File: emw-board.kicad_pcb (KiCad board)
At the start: 2 copper layers, 49.5 x 48.3 mm, 37 parts, among them P1 1WIRE, P2 BATT, P3 CONN_01X06, P4 SWDN, P5 CONS, P6 OLED, P7 CONN_01X07, SW1 B3S-1000, SW2 B3S-1000, U1 MAX604CSA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

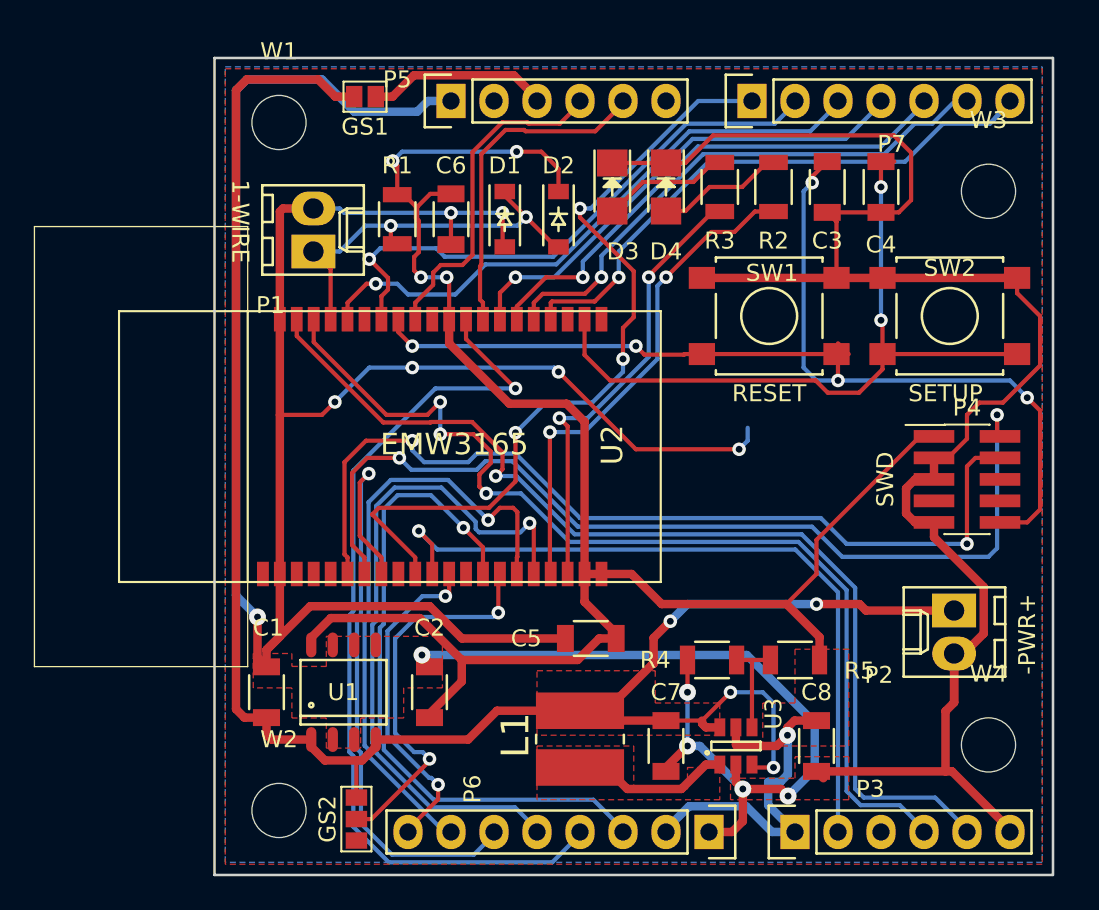
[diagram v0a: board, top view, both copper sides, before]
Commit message: Add micro-usb connector (for power only).
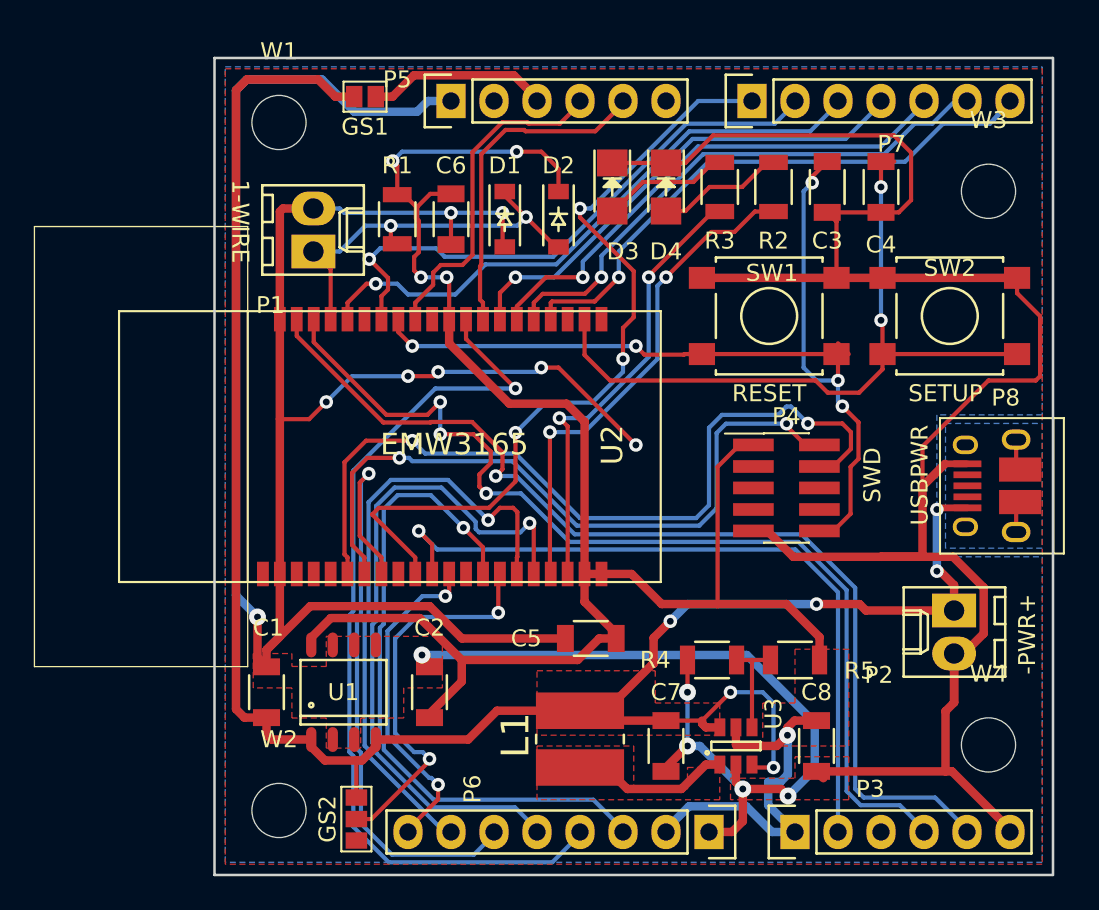
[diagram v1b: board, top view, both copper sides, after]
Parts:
- added P8: USB_OTG, Connect:USB_Micro-B_10103594-0001LF, F.Cu at (160.3, 78.6)
- GS1: footprint GS2 -> Connect:GS2
- GS2: footprint GS3 -> Connect:GS3
- moved P4 10.7 mm to (148.1, 78.7)
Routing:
- net Net-(P4-Pad2): track 57.0 -> 41.6 mm
- net Net-(C3-Pad1): track 66.0 -> 55.6 mm
- net GND: track 301.5 -> 310.2 mm, vias 12 -> 13
- net +BATT: track 115.5 -> 123.9 mm, vias 4 -> 6
- net Net-(P4-Pad4): track 54.0 -> 48.3 mm
- net Net-(P8-Pad6): track 0.00 -> 3.74 mm
- net +3V3: track 130.7 -> 127.5 mm
- added copper zone on B.Cu, net Net-(P8-Pad6)
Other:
- board text added: "USBPWR"
